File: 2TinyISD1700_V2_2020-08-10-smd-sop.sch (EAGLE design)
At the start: 18 parts, among them IC3 LM317MDT, U1 ATTINY4313-SU

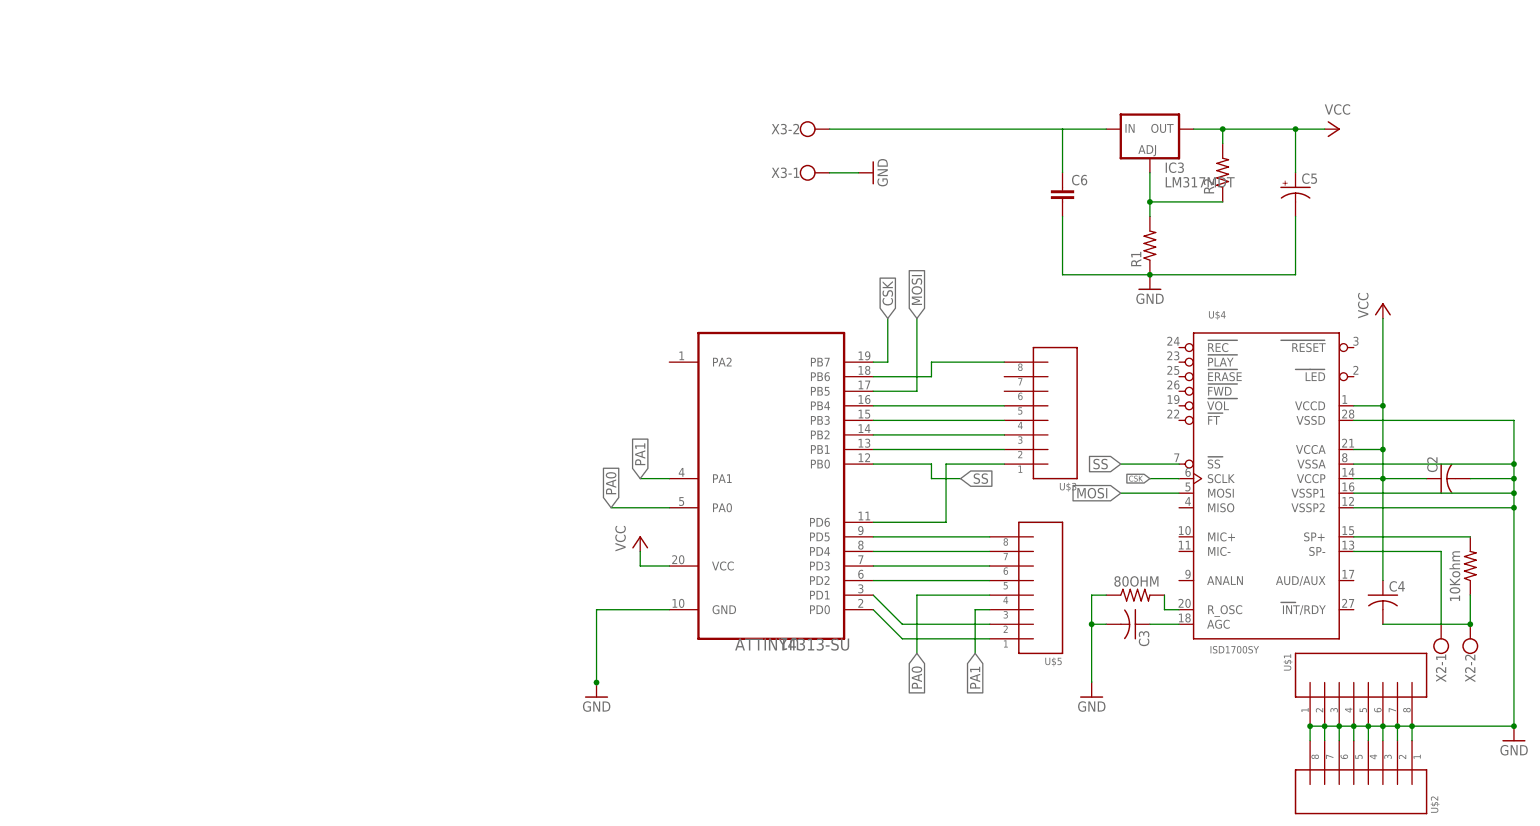
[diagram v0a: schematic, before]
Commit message: added css connection
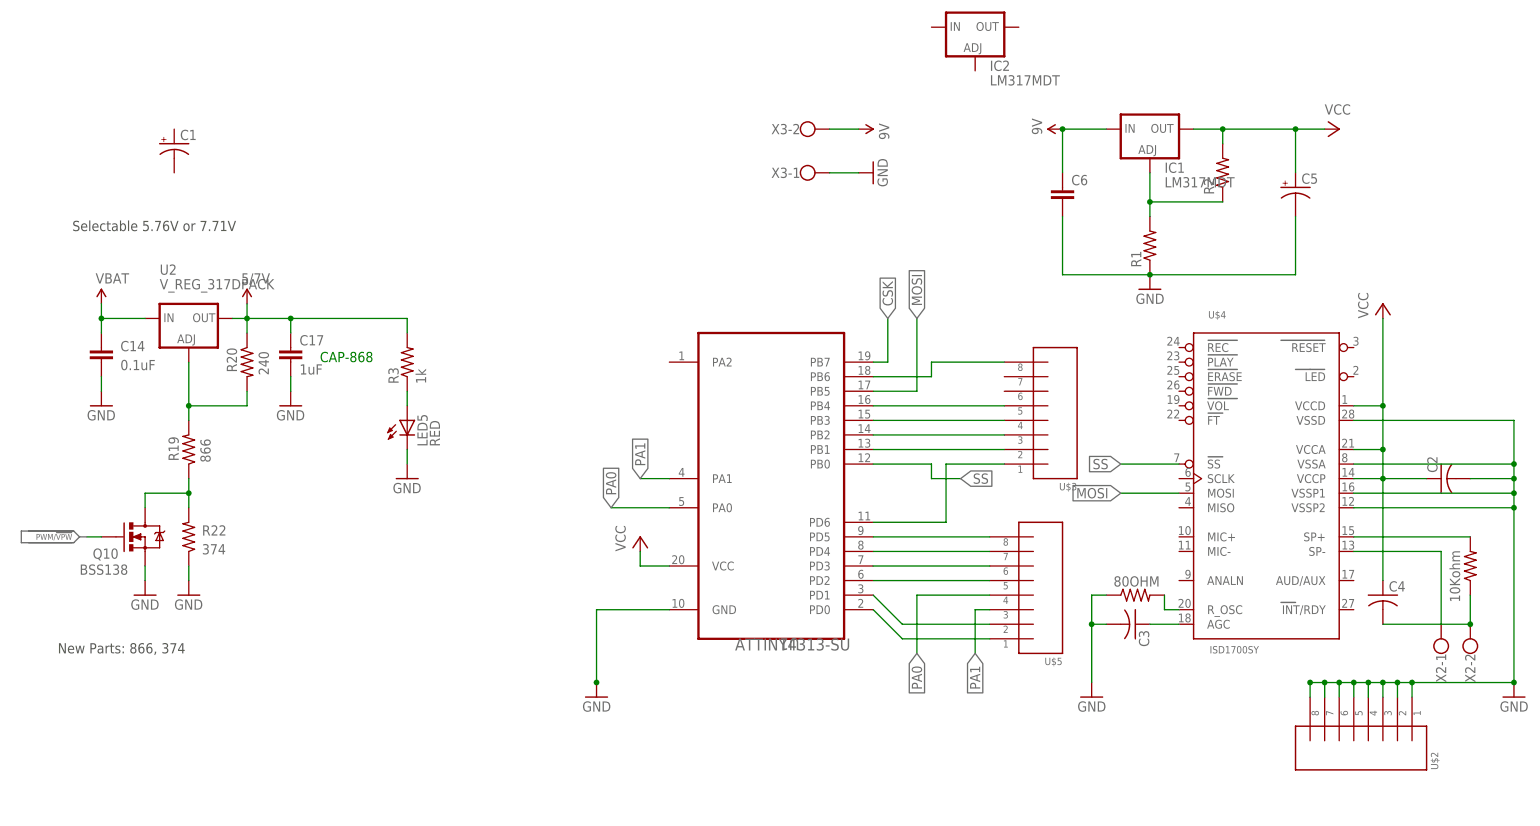
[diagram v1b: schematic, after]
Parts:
- removed U$1: 8PIN_HEADER, arduino:8PIN_HEADER
- added C1: (no value), SparkFun2:CAP_POL1206
- added C14: 0.1uF, SparkFun:CAP0402-CAP
- added C17: 1uF, SparkFun:CAP0402-CAP
- added IC2: LM317MDT, v-reg:LM317MDT
- added LED5: RED, SparkFun:LED0603
- added Q10: BSS138, SparkFun:MOSFET-NCHANNELSMD
- added R19: 866, SparkFun:RESISTOR0402-RES
- added R20: 240, SparkFun:RESISTOR0402-RES
- added R22: 374, SparkFun:RESISTOR0402-RES
- added R3: 1k, SparkFun:RESISTOR0402-RES
- added U2: V_REG_317DPACK, SparkFun:V_REG_317DPACK
- R1, R2: device SparkFun:RESISTOR1206 -> SparkFun2:RESISTOR
- renumbered IC3 to IC1
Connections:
- net N$28 renamed 5V
- new net N$10: R19.2, R20.2, U2.ADJ
- new net N$22: Q10.D, R19.1, R22.2
- new net N$32: LED5.A, R3.1
- new net PWM/!VPW: Q10.G
- new net VBAT: C14.1, U2.IN
- net CSK: no longer U$4.SCLK
- net GND: now also C14.2, C17.2, LED5.C, Q10.S, R22.1; no longer U$1.P$1, U$1.P$2, U$1.P$3, U$1.P$4, U$1.P$5, U$1.P$6, U$1.P$7, U$1.P$8
- net VCC: now also C17.1, R20.1, R3.2, U2.OUT
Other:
- note added: "CAP-868"
- note added: "New Parts: 866, 374"
- note added: "Selectable 5.76V or 7.71V"
- moved on the sheet: U$2
